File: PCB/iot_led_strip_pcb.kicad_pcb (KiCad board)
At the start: 4 copper layers, 57 x 56 mm, 80 parts, among them J1 Screw_Terminal_01x03, J2 Screw_Terminal_01x03, J3 GT-USB-7010ASV, J4 Barrel_Jack_Switch_Pin3Ring, J5 TC2050-JTAG, J7 PWR_HEADER, SW1 RESET, SW2 FLASH, SW3 SW_SPDT, SW4 SW_SPDT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

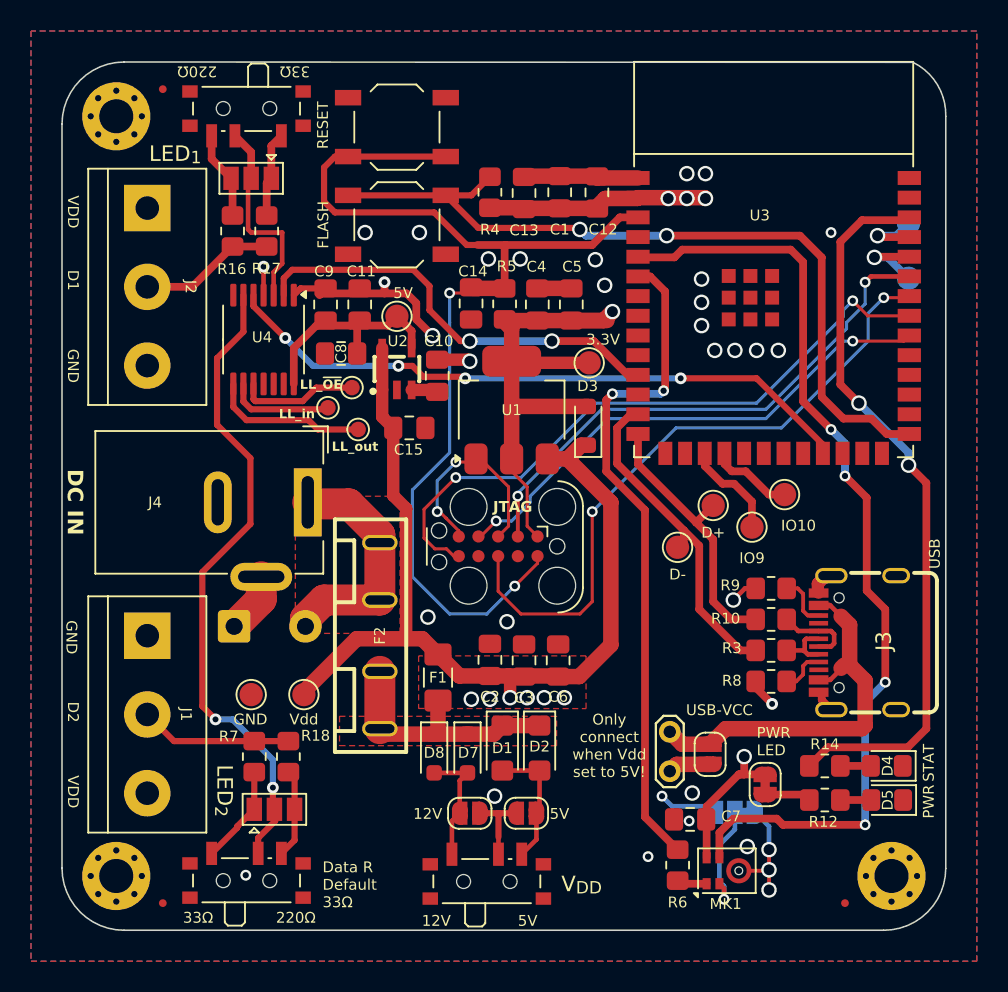
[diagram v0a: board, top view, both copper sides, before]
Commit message: v3.2 changes
* Removed PTC fuse, since that caused issues on the last one
* Other minor changes (that i've forgotten)
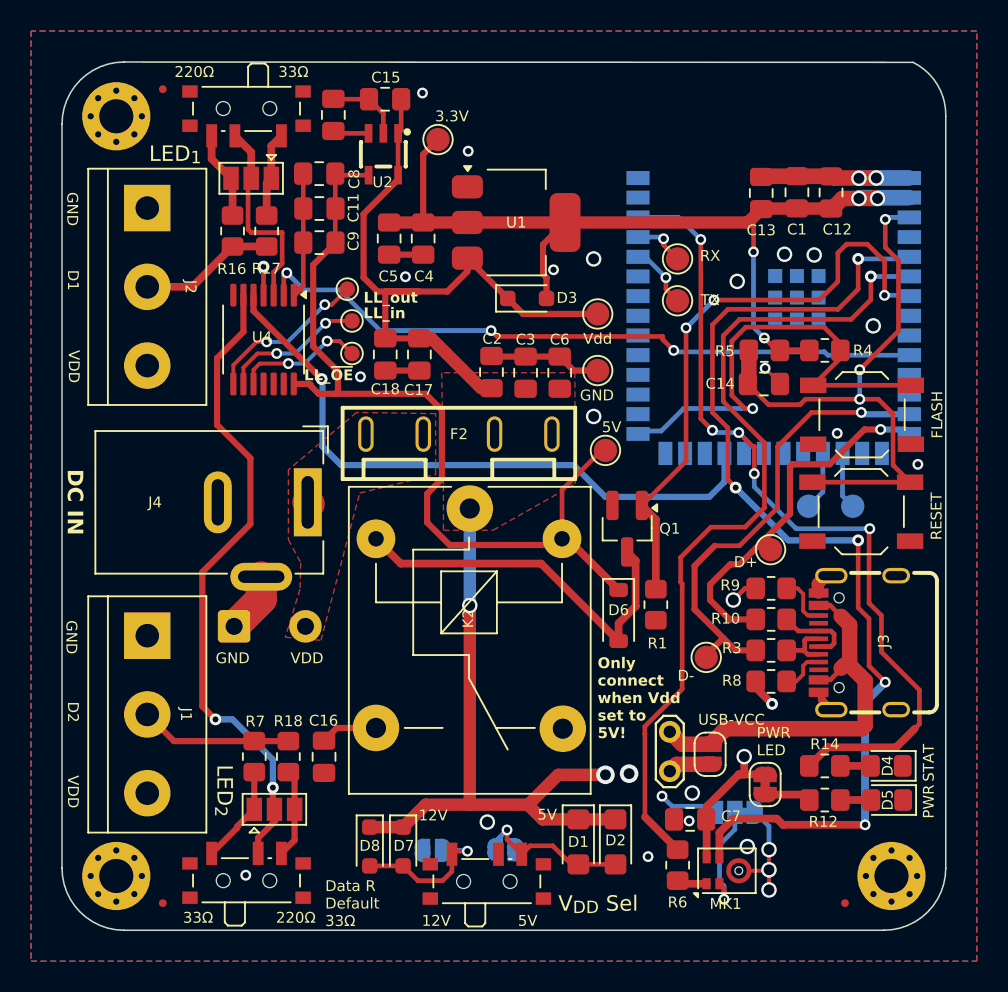
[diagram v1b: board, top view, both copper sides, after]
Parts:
- removed F1: 36V 1A Polyfuse, Fuse:Fuse_1206_3216Metric_Pad1.42x1.75mm_HandSolder
- removed J5: TC2050-JTAG, jmux-footprints:Tag-Connect_TC2050-IDC-FP_2x05_P1.27mm_Vertical
- added C16: 10uF, Capacitor_SMD:C_0805_2012Metric_Pad1.18x1.45mm_HandSolder, F.Cu at (135.9, 104.8)
- added C17: 10uF, Capacitor_SMD:C_0805_2012Metric_Pad1.18x1.45mm_HandSolder, F.Cu at (142.1, 78.9)
- added C18: 100nF, Capacitor_SMD:C_0805_2012Metric_Pad1.18x1.45mm_HandSolder, F.Cu at (139.8, 78.9)
- added D6: 1N4148W, Diode_SMD:D_SOD-123, F.Cu at (154.9, 95.7)
- added K2: SANYOU_SRD_Form_C, Relay_THT:Relay_SPDT_SANYOU_SRD_Series_Form_C, F.Cu at (145.3, 88.8)
- added Q1: AO3400A, Package_TO_SOT_SMD:SOT-23_Handsoldering, F.Cu at (155.4, 90.1)
- added R1: 10k, Resistor_SMD:R_0805_2012Metric_Pad1.20x1.40mm_HandSolder, F.Cu at (157.3, 95.0)
- J3: value GT-USB-7010ASV -> GT-USB-7010ASV
- JP4: value 12V TVS DISCON. -> 5V TVS DISCON.; moved to B.Cu
- JP8, TP8, TP9, U3: moved to B.Cu
- TP6, TP7: moved to F.Cu
- moved SW1 38.9 mm to (170.6, 89.0), turned to 180 degrees
- moved SW2 32.4 mm to (170.6, 82.8)
- moved TP1 31.0 mm to (153.6, 76.2)
- moved TP3 30.6 mm to (153.6, 79.9)
- moved R4 23.9 mm to (168.2, 78.6), turned to 180 degrees
- moved C15 21.3 mm to (139.8, 62.4), turned to 180 degrees
- moved C14 19.6 mm to (164.3, 80.8), turned to 0 degrees
- moved C2 18.6 mm to (146.7, 80.0)
- moved C3 18.6 mm to (148.9, 80.0)
- moved C6 18.6 mm to (151.1, 80.0)
- moved C10 18.1 mm to (136.5, 63.4)
- moved TP2 17.4 mm to (143.2, 65.0)
- moved R5 17.0 mm to (164.3, 78.6), turned to 180 degrees
- moved TP10 16.0 mm to (154.1, 85.0)
- moved C1 15.3 mm to (166.4, 68.4)
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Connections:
- C15 pad 1: VDD -> /Power_and_board/Vdd_in_fuse
- C2 pad 1: VDD -> /Power_and_board/Vdd_in_fuse
- C3 pad 1: VDD -> /Power_and_board/Vdd_in_fuse
- C6 pad 1: VDD -> /Power_and_board/Vdd_in_fuse
- D3 pad 1: VDD -> /Power_and_board/Vdd_in_fuse
- J2 pad 1: VDD -> Earth
- J2 pad 3: Earth -> VDD
- JP1 pad 2: VDD -> /Power_and_board/Vdd_in_fuse
- JP3 pad 2: VDD -> /Power_and_board/Vdd_in_fuse
- TP1 pad 1: VDD -> /Power_and_board/Vdd_in_fuse
- U1 pad 3: VDD -> /Power_and_board/Vdd_in_fuse
- U2 pad 1: VDD -> /Power_and_board/Vdd_in_fuse
- U2 pad 5: VDD -> /Power_and_board/Vdd_in_fuse
- U3 pad 10: unconnected-(U3-GPIO17/U1TXD/ADC2_CH6/DAC_1-Pad10) -> /LV_DIN1
- U3 pad 11: /LV_DIN1 -> unconnected-(U3-GPIO18/U1RXD/ADC2_CH7/DAC_2/CLK_OUT3-Pad11)
- U3 pad 32: /TCK -> unconnected-(U3-MTCK/GPIO39/CLK_OUT3-Pad32)
- U3 pad 33: /TDO -> unconnected-(U3-MTDO/GPIO40/CLK_OUT2-Pad33)
- U3 pad 34: /TDI -> unconnected-(U3-MTDI/GPIO41/CLK_OUT1-Pad34)
- U3 pad 35: /TMS -> unconnected-(U3-MTMS/GPIO42-Pad35)
- U3 pad 7: unconnected-(U3-GPIO7/TOUCH7/ADC1_CH6-Pad7) -> RELAY_PIN
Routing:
- net VDD: track 81.0 -> 3.69 mm, vias 6 -> 0
- net /Power_and_board/Vdd_in_fuse: track 16.6 -> 92.7 mm, vias 0 -> 3
- net +5V: track 14.2 -> 56.9 mm
- net /TDI: track 42.2 -> 0.00 mm, vias 2 -> 0
- net /TDO: track 42.1 -> 0.00 mm, vias 2 -> 0
- net RELAY_PIN: track 0.00 -> 38.7 mm, vias 0 -> 3
- net /TMS: track 34.9 -> 0.00 mm, vias 2 -> 0
- net /TCK: track 33.3 -> 0.00 mm, vias 2 -> 0
- net ~{RST}: track 69.1 -> 38.3 mm, vias 2 -> 3
- net Net-(D6-A): track 0.00 -> 24.8 mm
- net +3.3V: track 60.7 -> 83.0 mm
- net BOOT: track 51.2 -> 29.6 mm, vias 2 -> 1
- net /LV_DIN1: track 27.9 -> 44.0 mm, vias 2 -> 3
- net /Power_and_board/Vdd IN: track 15.5 -> 0.14 mm
- net /MIC_DATA: track 43.4 -> 54.1 mm, vias 2 -> 1
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- removed copper zone on F.Cu, net VDD
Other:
- board text added: "${REVISION}-${DATE_CODE}"
- board text added: "Driver ID:"
- board text added: "IoT LED Driver"
- board text added: "JLCJLCJLCJLC"
- board text added: "V_{DD} Sel"
- board text removed: "${REVISION}-0424"
- board text removed: "IoT LED Driver HW"
- board text removed: "V_{DD}"
